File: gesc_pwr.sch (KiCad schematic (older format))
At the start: 48 parts, among them J10 PHASE_C, J11 PHASE_B, J12 NTC, J9 PHASE_A, Q1 TPH2R608NH,L1Q, Q2 TPH2R608NH,L1Q, Q3 TPH2R608NH,L1Q, Q4 TPH2R608NH,L1Q, Q5 TPH2R608NH,L1Q, Q6 TPH2R608NH,L1Q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

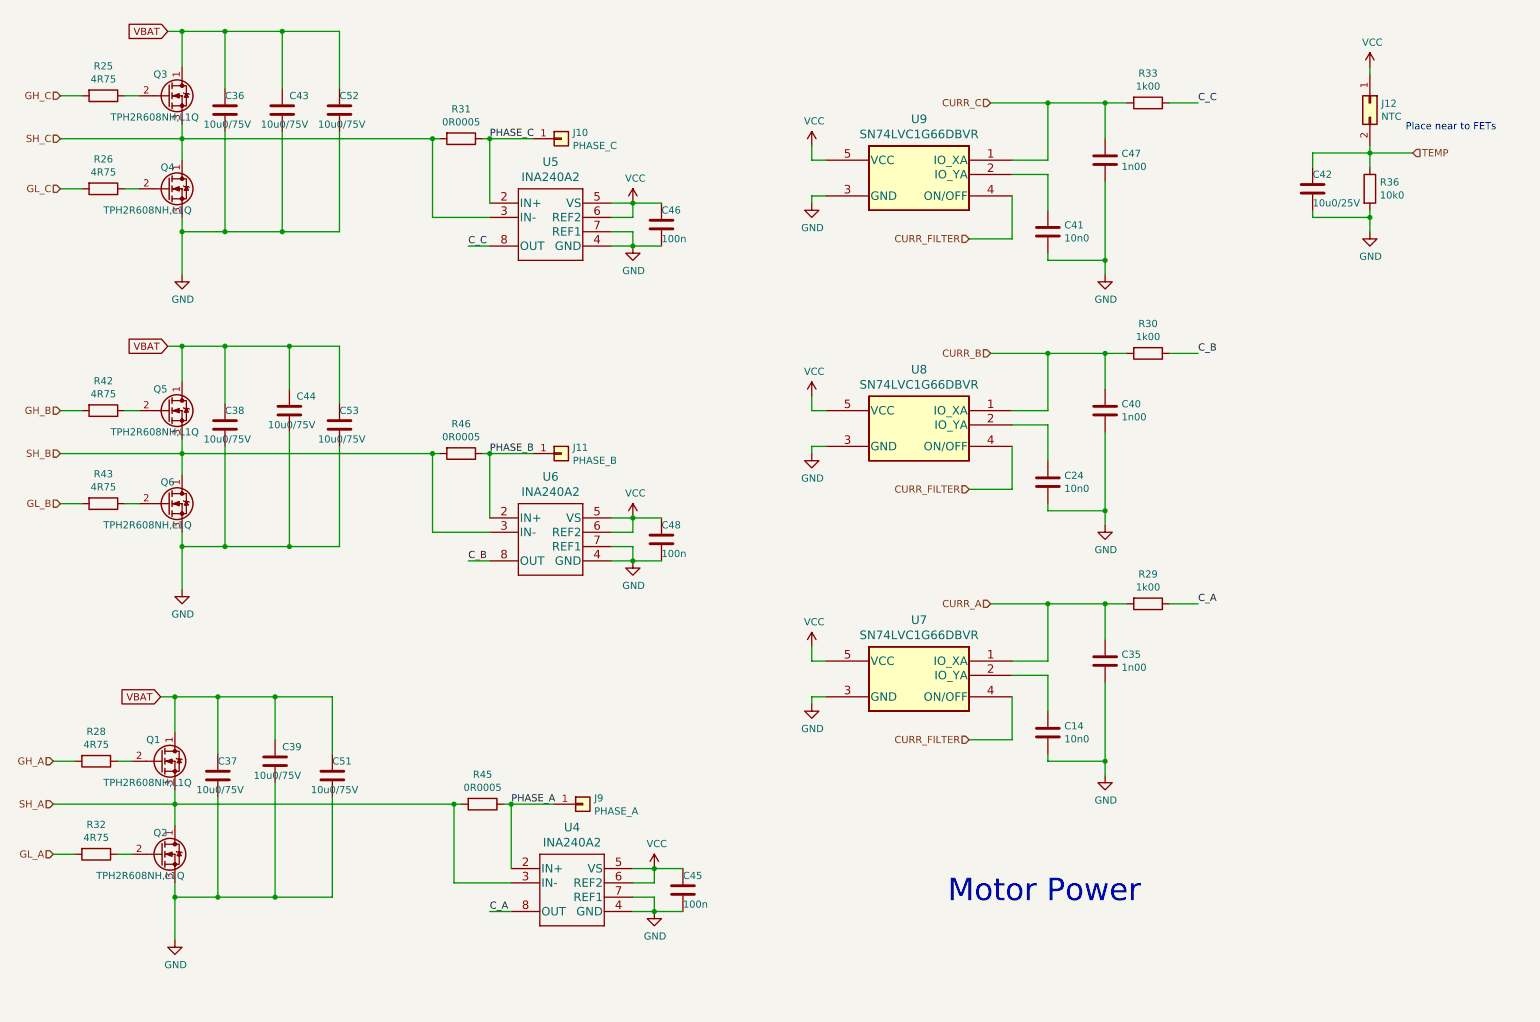
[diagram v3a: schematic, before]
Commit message: - remove solder-mask from bottom layer
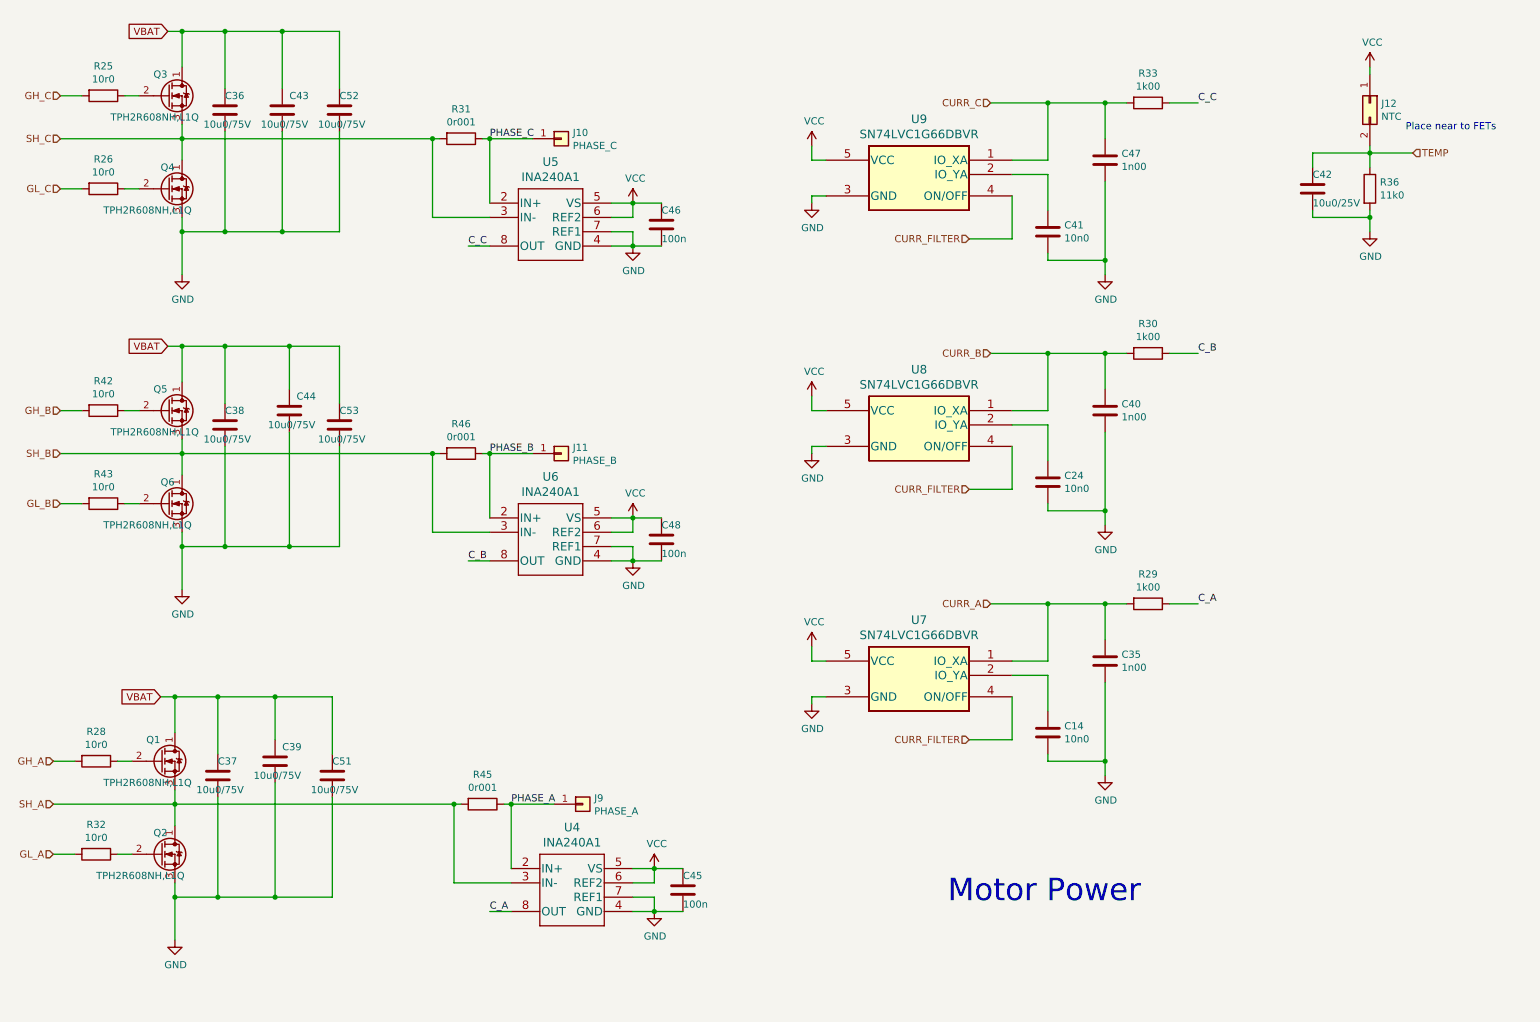
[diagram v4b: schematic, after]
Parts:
- C36: LCSC (none) -> C15850
- R25, R26, R28, R32, R42, R43: value 4R75 -> 10r0
- R31, R45, R46: value 0R0005 -> 0r001
- R36: value 10k0 -> 11k0
- U4, U5, U6: value INA240A2 -> INA240A1; LCSC (none) -> C93965
- U7, U8, U9: LCSC (none) -> C133643
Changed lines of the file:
@@
 P 1200 1950
 F 0 "R26" V 993 1950 50  0000 C CNN
-F 1 "4R75" V 1084 1950 50  0000 C CNN
+F 1 "10r0" V 1084 1950 50  0000 C CNN
 F 2 "Resistor_SMD:R_0805_2012Metric" V 1130 1950 50  0001 C CNN
 F 3 "~" H 1200 1950 50  0001 C CNN
@@
 P 1200 1300
 F 0 "R25" V 993 1300 50  0000 C CNN
-F 1 "4R75" V 1084 1300 50  0000 C CNN
+F 1 "10r0" V 1084 1300 50  0000 C CNN
 F 2 "Resistor_SMD:R_0805_2012Metric" V 1130 1300 50  0001 C CNN
 F 3 "~" H 1200 1300 50  0001 C CNN
@@
 F 2 "Capacitor_SMD:C_1210_3225Metric" H 2088 1250 50  0001 C CNN
 F 3 "~" H 2050 1400 50  0001 C CNN
+F 4 "C15850" H 2050 1400 50  0001 C CNN "LCSC"
 	1    2050 1400
 	1    0    0    -1
@@
 P 10050 1950
 F 0 "R36" H 10120 1996 50  0000 L CNN
-F 1 "10k0" H 10120 1905 50  0000 L CNN
+F 1 "11k0" H 10120 1905 50  0000 L CNN
 F 2 "Resistor_SMD:R_0805_2012Metric" V 9980 1950 50  0001 C CNN
 F 3 "~" H 10050 1950 50  0001 C CNN
@@
 P 3700 1600
 F 0 "R31" V 3493 1600 50  0000 C CNN
-F 1 "0R0005" V 3584 1600 50  0000 C CNN
+F 1 "0r001" V 3584 1600 50  0000 C CNN
 F 2 "Resistor_SMD:R_2512_6332Metric" V 3630 1600 50  0001 C CNN
 F 3 "~" H 3700 1600 50  0001 C CNN
@@
 F 2 "gesc:M74VHC1GT66DTT1G" H 6750 5250 60  0001 C CNN
 F 3 "" H 6250 5450 60  0000 C CNN
+F 4 "C133643" H 6250 5450 50  0001 C CNN "LCSC"
 	1    6250 5450
 	1    0    0    -1
@@
 F 2 "gesc:M74VHC1GT66DTT1G" H 6750 3500 60  0001 C CNN
 F 3 "" H 6250 3700 60  0000 C CNN
+F 4 "C133643" H 6250 3700 50  0001 C CNN "LCSC"
 	1    6250 3700
 	1    0    0    -1
@@
 F 2 "gesc:M74VHC1GT66DTT1G" H 6750 1750 60  0001 C CNN
 F 3 "" H 6250 1950 60  0000 C CNN
+F 4 "C133643" H 6250 1950 50  0001 C CNN "LCSC"
 	1    6250 1950
 	1    0    0    -1
@@
 P 4600 2450
 F 0 "U5" H 4325 3138 60  0000 C CNN
-F 1 "INA240A2" H 4325 3032 60  0000 C CNN
+F 1 "INA240A1" H 4325 3032 60  0000 C CNN
 F 2 "gesc:INA240A1QPWRQ1" H 4350 2400 60  0001 C CNN
 F 3 "" H 4600 2450 60  0000 C CNN
+F 4 "C93965" H 4600 2450 50  0001 C CNN "LCSC"
 	1    4600 2450
 	1    0    0    -1
@@
 P 1200 4150
 F 0 "R43" V 993 4150 50  0000 C CNN
-F 1 "4R75" V 1084 4150 50  0000 C CNN
+F 1 "10r0" V 1084 4150 50  0000 C CNN
 F 2 "Resistor_SMD:R_0805_2012Metric" V 1130 4150 50  0001 C CNN
 F 3 "~" H 1200 4150 50  0001 C CNN
@@
 P 1200 3500
 F 0 "R42" V 993 3500 50  0000 C CNN
-F 1 "4R75" V 1084 3500 50  0000 C CNN
+F 1 "10r0" V 1084 3500 50  0000 C CNN
 F 2 "Resistor_SMD:R_0805_2012Metric" V 1130 3500 50  0001 C CNN
 F 3 "~" H 1200 3500 50  0001 C CNN
@@
 P 3700 3800
 F 0 "R46" V 3493 3800 50  0000 C CNN
-F 1 "0R0005" V 3584 3800 50  0000 C CNN
+F 1 "0r001" V 3584 3800 50  0000 C CNN
 F 2 "Resistor_SMD:R_2512_6332Metric" V 3630 3800 50  0001 C CNN
 F 3 "~" H 3700 3800 50  0001 C CNN
@@
 P 4600 4650
 F 0 "U6" H 4325 5338 60  0000 C CNN
-F 1 "INA240A2" H 4325 5232 60  0000 C CNN
+F 1 "INA240A1" H 4325 5232 60  0000 C CNN
 F 2 "gesc:INA240A1QPWRQ1" H 4350 4600 60  0001 C CNN
 F 3 "" H 4600 4650 60  0000 C CNN
+F 4 "C93965" H 4600 4650 50  0001 C CNN "LCSC"
 	1    4600 4650
 	1    0    0    -1
@@
 P 1150 6600
 F 0 "R32" V 943 6600 50  0000 C CNN
-F 1 "4R75" V 1034 6600 50  0000 C CNN
+F 1 "10r0" V 1034 6600 50  0000 C CNN
 F 2 "Resistor_SMD:R_0805_2012Metric" V 1080 6600 50  0001 C CNN
 F 3 "~" H 1150 6600 50  0001 C CNN
@@
 P 1150 5950
 F 0 "R28" V 943 5950 50  0000 C CNN
-F 1 "4R75" V 1034 5950 50  0000 C CNN
+F 1 "10r0" V 1034 5950 50  0000 C CNN
 F 2 "Resistor_SMD:R_0805_2012Metric" V 1080 5950 50  0001 C CNN
 F 3 "~" H 1150 5950 50  0001 C CNN
@@
 P 3850 6250
 F 0 "R45" V 3643 6250 50  0000 C CNN
-F 1 "0R0005" V 3734 6250 50  0000 C CNN
+F 1 "0r001" V 3734 6250 50  0000 C CNN
 F 2 "Resistor_SMD:R_2512_6332Metric" V 3780 6250 50  0001 C CNN
 F 3 "~" H 3850 6250 50  0001 C CNN
@@
 P 4750 7100
 F 0 "U4" H 4475 7788 60  0000 C CNN
-F 1 "INA240A2" H 4475 7682 60  0000 C CNN
+F 1 "INA240A1" H 4475 7682 60  0000 C CNN
 F 2 "gesc:INA240A1QPWRQ1" H 4500 7050 60  0001 C CNN
 F 3 "" H 4750 7100 60  0000 C CNN
+F 4 "C93965" H 4750 7100 50  0001 C CNN "LCSC"
 	1    4750 7100
 	1    0    0    -1

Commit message: JLC ready
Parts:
- removed Q1, Q2, Q4, Q5, Q6: TPH2R608NH,L1Q, gesc:TRANS_TPHR8504PL-3PIN, symbol gesc:TPH2R506PL
- removed Q3: TPH2R608NH,L1Q, gesc:TRANS_TPHR8504PL-3PIN, symbol gesc:TPH2R608NH
- added Q1, Q2, Q3, Q4, Q5, Q6: BSC070N10NS5, Package_TO_SOT_SMD:TDSON-8-1, symbol Transistor_FET:BSC070N10NS5
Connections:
- net GND: now also Q2.1 (S), Q2.2 (S), Q2.3 (S), Q4.1 (S), Q4.2 (S), Q4.3 (S), Q6.1 (S), Q6.2 (S), Q6.3 (S)
- net SH_A: now also Q1.1 (S), Q1.2 (S), Q1.3 (S), Q2.5 (D)
- net SH_B: now also Q5.1 (S), Q5.2 (S), Q5.3 (S), Q6.5 (D)
- net SH_C: now also Q3.1 (S), Q3.2 (S), Q3.3 (S), Q4.5 (D)
- net VBAT: now also Q1.5 (D), Q3.5 (D), Q5.5 (D)
- net at R26.1: now also Q4.4 (G)
- net at R25.1: now also Q3.4 (G)
- net at R43.1: now also Q6.4 (G)
- net at R42.1: now also Q5.4 (G)
- net at R32.1: now also Q2.4 (G)
- net at R28.1: now also Q1.4 (G)
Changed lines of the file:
@@
 Wire Wire Line
 	6150 2000 6150 2050
-$Comp
-L gesc:TPH2R608NH Q3
-U 1 1 5E3D365F
-P 1650 1300
-F 0 "Q3" H 1550 1450 50  0000 L CNN
-F 1 "TPH2R608NH,L1Q" H 1250 1150 50  0000 L CNN
-F 2 "gesc:TRANS_TPHR8504PL-3PIN" H 1650 1300 50  0001 C CIN
-F 3 "" H 1650 1300 50  0001 L CNN
-F 4 "C146377" H 0   0   50  0001 C CNN "LCSC"
-F 5 "TPH2R608NH" H 0   0   50  0001 C CNN "Partnumber"
-	1    1650 1300
-	1    0    0    -1
-$EndComp
-$Comp
-L gesc:TPH2R506PL Q4
-U 1 1 5E3D3778
-P 1650 1950
-F 0 "Q4" H 1600 2100 50  0000 L CNN
-F 1 "TPH2R608NH,L1Q" H 1200 1800 50  0000 L CNN
-F 2 "gesc:TRANS_TPHR8504PL-3PIN" H 1650 1950 50  0001 C CIN
-F 3 "" H 1650 1950 50  0001 L CNN
-F 4 "C146377" H 0   0   50  0001 C CNN "LCSC"
-F 5 "TPH2R608NH" H 0   0   50  0001 C CNN "Partnumber"
-	1    1650 1950
-	1    0    0    -1
-$EndComp
 Connection ~ 2050 2250
 Connection ~ 2050 850
@@
 PHASE_B
 $Comp
-L gesc:TPH2R506PL Q5
-U 1 1 5E6023E2
-P 1650 3500
-F 0 "Q5" H 1550 3650 50  0000 L CNN
-F 1 "TPH2R608NH,L1Q" H 1250 3350 50  0000 L CNN
-F 2 "gesc:TRANS_TPHR8504PL-3PIN" H 1650 3500 50  0001 C CIN
-F 3 "" H 1650 3500 50  0001 L CNN
-F 4 "C146377" H 0   0   50  0001 C CNN "LCSC"
-F 5 "TPH2R608NH" H 0   0   50  0001 C CNN "Partnumber"
-	1    1650 3500
-	1    0    0    -1
-$EndComp
-$Comp
-L gesc:TPH2R506PL Q6
-U 1 1 5E6023E8
-P 1650 4150
-F 0 "Q6" H 1600 4300 50  0000 L CNN
-F 1 "TPH2R608NH,L1Q" H 1200 4000 50  0000 L CNN
-F 2 "gesc:TRANS_TPHR8504PL-3PIN" H 1650 4150 50  0001 C CIN
-F 3 "" H 1650 4150 50  0001 L CNN
-F 4 "C146377" H 0   0   50  0001 C CNN "LCSC"
-F 5 "TPH2R608NH" H 0   0   50  0001 C CNN "Partnumber"
-	1    1650 4150
-	1    0    0    -1
-$EndComp
-$Comp
 L Device:C C44
 U 1 1 5E60241D
@@
 Text Label 4050 6250 0    50   ~ 0
 PHASE_A
-$Comp
-L gesc:TPH2R506PL Q1
-U 1 1 5E60A8BA
-P 1600 5950
-F 0 "Q1" H 1500 6100 50  0000 L CNN
-F 1 "TPH2R608NH,L1Q" H 1200 5800 50  0000 L CNN
-F 2 "gesc:TRANS_TPHR8504PL-3PIN" H 1600 5950 50  0001 C CIN
-F 3 "" H 1600 5950 50  0001 L CNN
-F 4 "C146377" H 0   0   50  0001 C CNN "LCSC"
-F 5 "TPH2R608NH" H 0   0   50  0001 C CNN "Partnumber"
-	1    1600 5950
-	1    0    0    -1
-$EndComp
-$Comp
-L gesc:TPH2R506PL Q2
-U 1 1 5E60A8C0
-P 1600 6600
-F 0 "Q2" H 1550 6750 50  0000 L CNN
-F 1 "TPH2R608NH,L1Q" H 1150 6450 50  0000 L CNN
-F 2 "gesc:TRANS_TPHR8504PL-3PIN" H 1600 6600 50  0001 C CIN
-F 3 "" H 1600 6600 50  0001 L CNN
-F 4 "C146377" H 0   0   50  0001 C CNN "LCSC"
-F 5 "TPH2R608NH" H 0   0   50  0001 C CNN "Partnumber"
-	1    1600 6600
-	1    0    0    -1
-$EndComp
 $Comp
 L Device:C C39
@@
 Wire Wire Line
 	2800 6200 2800 6900
+$Comp
+L Transistor_FET:BSC070N10NS5 Q3
+U 1 1 601290B0
+P 1650 1300
+F 0 "Q3" H 1854 1346 50  0000 L CNN
+F 1 "BSC070N10NS5" H 1854 1255 50  0000 L CNN
+F 2 "Package_TO_SOT_SMD:TDSON-8-1" H 1850 1225 50  0001 L CIN
+F 3 "http://www.infineon.com/dgdl/Infineon-BSC070N10NS5-DS-v02_01-EN.pdf?fileId=5546d4624a0bf290014a0fc62d9d6b3c" V 1650 1300 50  0001 L CNN
+	1    1650 1300
+	1    0    0    -1
+$EndComp
+$Comp
+L Transistor_FET:BSC070N10NS5 Q4
+U 1 1 60131502
+P 1650 1950
+F 0 "Q4" H 1854 1996 50  0000 L CNN
+F 1 "BSC070N10NS5" H 1854 1905 50  0000 L CNN
+F 2 "Package_TO_SOT_SMD:TDSON-8-1" H 1850 1875 50  0001 L CIN
+F 3 "http://www.infineon.com/dgdl/Infineon-BSC070N10NS5-DS-v02_01-EN.pdf?fileId=5546d4624a0bf290014a0fc62d9d6b3c" V 1650 1950 50  0001 L CNN
+	1    1650 1950
+	1    0    0    -1
+$EndComp
+$Comp
+L Transistor_FET:BSC070N10NS5 Q5
+U 1 1 60136E0E
+P 1650 3500
+F 0 "Q5" H 1854 3546 50  0000 L CNN
+F 1 "BSC070N10NS5" H 1854 3455 50  0000 L CNN
+F 2 "Package_TO_SOT_SMD:TDSON-8-1" H 1850 3425 50  0001 L CIN
+F 3 "http://www.infineon.com/dgdl/Infineon-BSC070N10NS5-DS-v02_01-EN.pdf?fileId=5546d4624a0bf290014a0fc62d9d6b3c" V 1650 3500 50  0001 L CNN
+	1    1650 3500
+	1    0    0    -1
+$EndComp
+$Comp
+L Transistor_FET:BSC070N10NS5 Q6
+U 1 1 601394AD
+P 1650 4150
+F 0 "Q6" H 1854 4196 50  0000 L CNN
+F 1 "BSC070N10NS5" H 1854 4105 50  0000 L CNN
+F 2 "Package_TO_SOT_SMD:TDSON-8-1" H 1850 4075 50  0001 L CIN
+F 3 "http://www.infineon.com/dgdl/Infineon-BSC070N10NS5-DS-v02_01-EN.pdf?fileId=5546d4624a0bf290014a0fc62d9d6b3c" V 1650 4150 50  0001 L CNN
+	1    1650 4150
+	1    0    0    -1
+$EndComp
+$Comp
+L Transistor_FET:BSC070N10NS5 Q1
+U 1 1 6013C3DE
+P 1600 5950
+F 0 "Q1" H 1804 5996 50  0000 L CNN
+F 1 "BSC070N10NS5" H 1804 5905 50  0000 L CNN
+F 2 "Package_TO_SOT_SMD:TDSON-8-1" H 1800 5875 50  0001 L CIN
+F 3 "http://www.infineon.com/dgdl/Infineon-BSC070N10NS5-DS-v02_01-EN.pdf?fileId=5546d4624a0bf290014a0fc62d9d6b3c" V 1600 5950 50  0001 L CNN
+	1    1600 5950
+	1    0    0    -1
+$EndComp
+$Comp
+L Transistor_FET:BSC070N10NS5 Q2
+U 1 1 6013F03F
+P 1600 6600
+F 0 "Q2" H 1804 6646 50  0000 L CNN
+F 1 "BSC070N10NS5" H 1804 6555 50  0000 L CNN
+F 2 "Package_TO_SOT_SMD:TDSON-8-1" H 1800 6525 50  0001 L CIN
+F 3 "http://www.infineon.com/dgdl/Infineon-BSC070N10NS5-DS-v02_01-EN.pdf?fileId=5546d4624a0bf290014a0fc62d9d6b3c" V 1600 6600 50  0001 L CNN
+	1    1600 6600
+	1    0    0    -1
+$EndComp
 $EndSCHEMATC

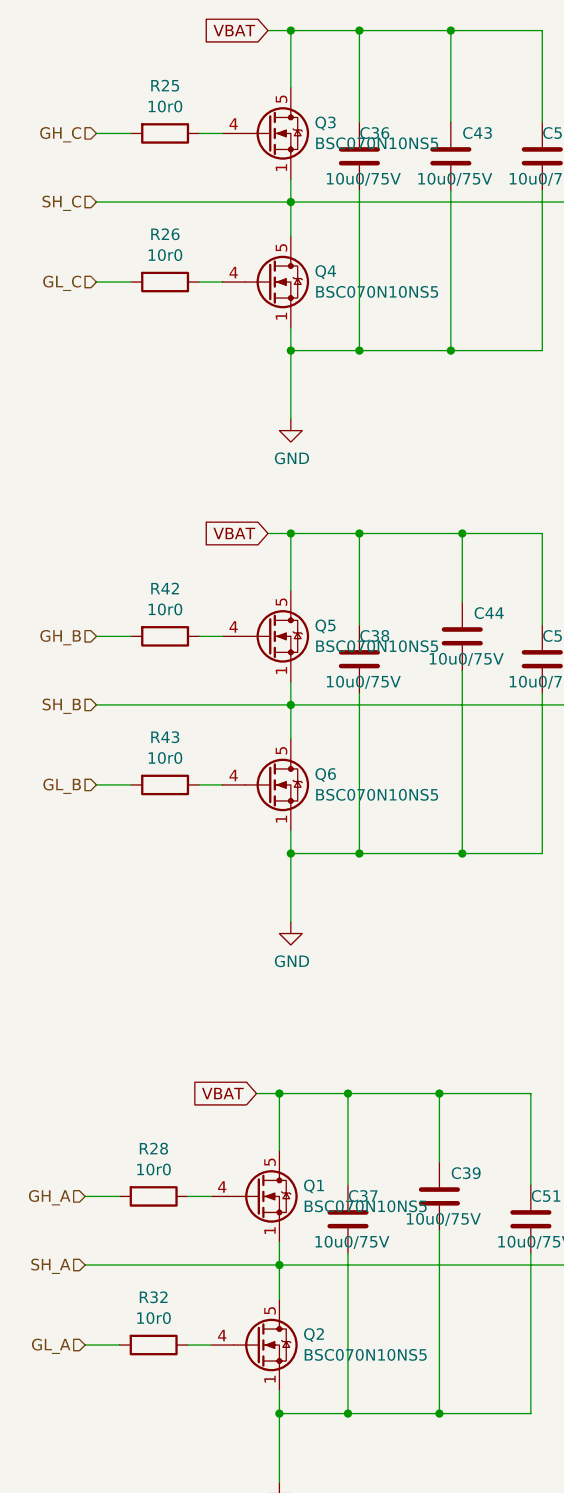
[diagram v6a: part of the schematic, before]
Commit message: |--- Add Schottky between phase and gnd at HS pin of LM5107 |--- Add 5R6 in phase line to HS pin of LM5107 |--- Change high side bypass cap to 10u/25V |--- Add 14V TVS diode parallel to high side bypass cap |--- Add one 12V TVS diode to 12V near driver |--- move gate tracks and back from side by side to on top of each other
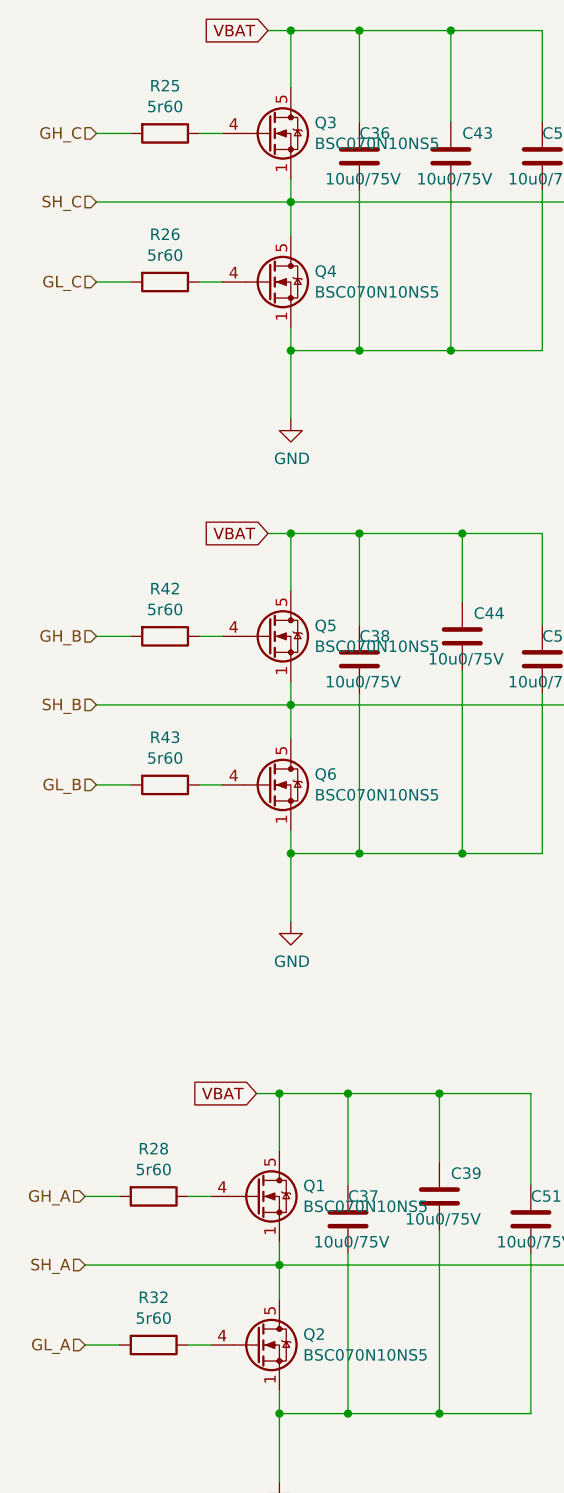
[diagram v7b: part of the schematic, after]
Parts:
- R25, R26, R28, R32, R42, R43: value 10r0 -> 5r60
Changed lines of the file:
@@
 P 1200 1950
 F 0 "R26" V 993 1950 50  0000 C CNN
-F 1 "10r0" V 1084 1950 50  0000 C CNN
+F 1 "5r60" V 1084 1950 50  0000 C CNN
 F 2 "Resistor_SMD:R_0805_2012Metric" V 1130 1950 50  0001 C CNN
 F 3 "~" H 1200 1950 50  0001 C CNN
@@
 P 1200 1300
 F 0 "R25" V 993 1300 50  0000 C CNN
-F 1 "10r0" V 1084 1300 50  0000 C CNN
+F 1 "5r60" V 1084 1300 50  0000 C CNN
 F 2 "Resistor_SMD:R_0805_2012Metric" V 1130 1300 50  0001 C CNN
 F 3 "~" H 1200 1300 50  0001 C CNN
@@
 P 1200 4150
 F 0 "R43" V 993 4150 50  0000 C CNN
-F 1 "10r0" V 1084 4150 50  0000 C CNN
+F 1 "5r60" V 1084 4150 50  0000 C CNN
 F 2 "Resistor_SMD:R_0805_2012Metric" V 1130 4150 50  0001 C CNN
 F 3 "~" H 1200 4150 50  0001 C CNN
@@
 P 1200 3500
 F 0 "R42" V 993 3500 50  0000 C CNN
-F 1 "10r0" V 1084 3500 50  0000 C CNN
+F 1 "5r60" V 1084 3500 50  0000 C CNN
 F 2 "Resistor_SMD:R_0805_2012Metric" V 1130 3500 50  0001 C CNN
 F 3 "~" H 1200 3500 50  0001 C CNN
@@
 P 1150 6600
 F 0 "R32" V 943 6600 50  0000 C CNN
-F 1 "10r0" V 1034 6600 50  0000 C CNN
+F 1 "5r60" V 1034 6600 50  0000 C CNN
 F 2 "Resistor_SMD:R_0805_2012Metric" V 1080 6600 50  0001 C CNN
 F 3 "~" H 1150 6600 50  0001 C CNN
@@
 P 1150 5950
 F 0 "R28" V 943 5950 50  0000 C CNN
-F 1 "10r0" V 1034 5950 50  0000 C CNN
+F 1 "5r60" V 1034 5950 50  0000 C CNN
 F 2 "Resistor_SMD:R_0805_2012Metric" V 1080 5950 50  0001 C CNN
 F 3 "~" H 1150 5950 50  0001 C CNN
